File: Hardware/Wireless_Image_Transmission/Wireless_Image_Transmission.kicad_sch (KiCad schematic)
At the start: 66 parts, among them IC1 EA3036QBR, IC10 HY2213-BB3A, IC11 HY2213-BB3A, IC12 HY2213-BB3A, IC13 HY2213-BB3A, IC2 TPS5450DDAR, Q2 AO3401A, Q3 AO3400, Q4 AO3400, Q5 AO3400, Q6 AO3400

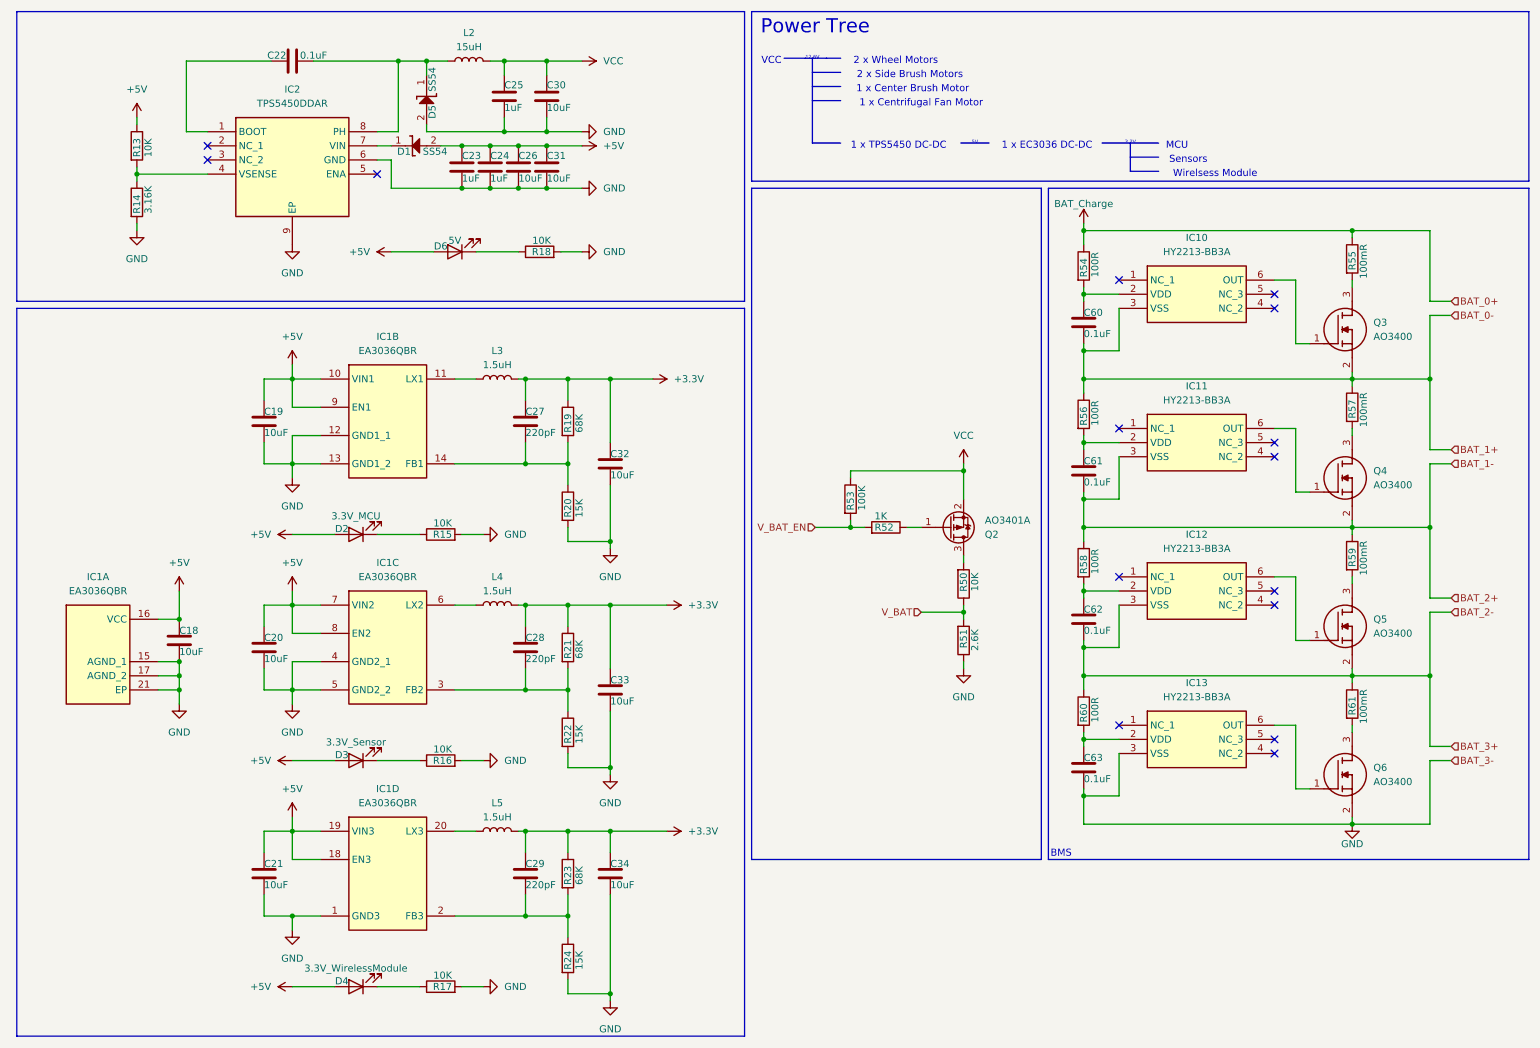
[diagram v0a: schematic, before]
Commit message: Add Image Transmission
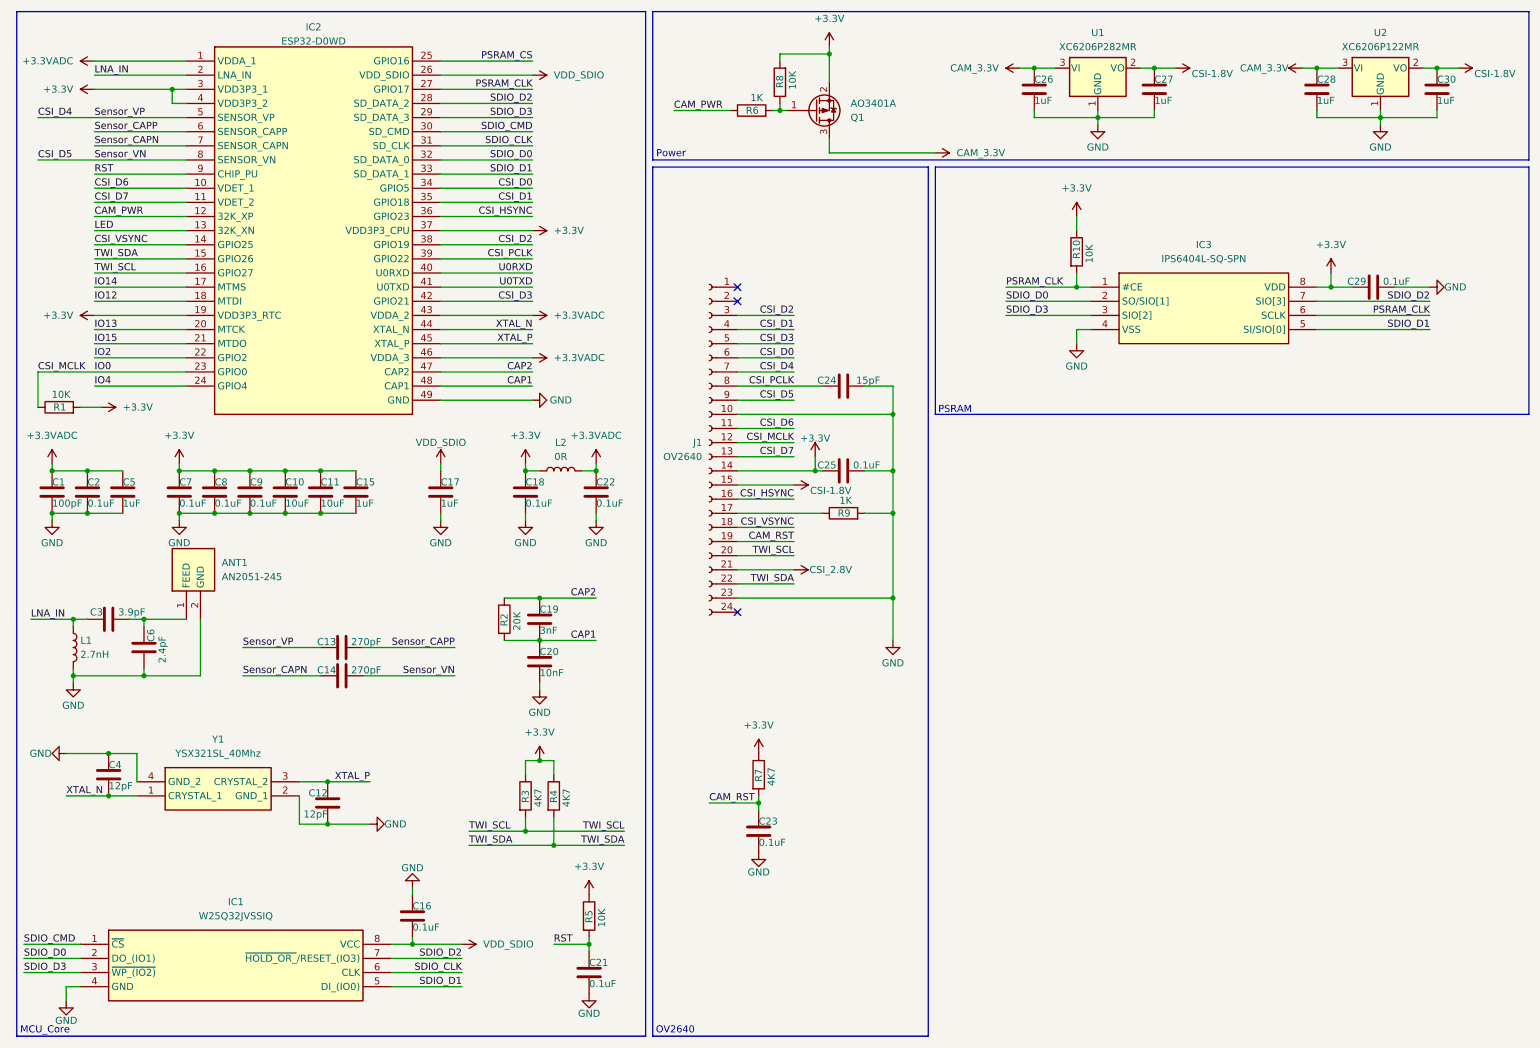
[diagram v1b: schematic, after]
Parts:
- removed C31, C32, C33, C34: 10uF, symbol Device:C
- removed C60, C61, C62, C63: 0.1uF, symbol Device:C
- removed D1, D5: SS54, DIOM5126X245N, symbol SamacSys_Parts:SS54
- removed D2: 3.3V_MCU, symbol Device:LED
- removed D3: 3.3V_Sensor, symbol Device:LED
- removed D4: 3.3V_WirelessModule, symbol Device:LED
- removed D6: 5V, symbol Device:LED
- removed IC1: EA3036QBR, QFN40P300X300X80-21N, symbol SamacSys_Parts:EA3036QBR
- removed IC10, IC11, IC12, IC13: HY2213-BB3A, SOT95P280X140-6N, symbol SamacSys_Parts:HY2213-BB3A
- removed IC2: TPS5450DDAR, SOIC127P600X170-9N, symbol SamacSys_Parts:TPS5450DDAR
- removed L3, L4, L5: 1.5uH, symbol Device:L
- removed Q2: AO3401A, Package_TO_SOT_SMD:SOT-23, symbol Transistor_FET:AO3401A
- removed Q3, Q4, Q5, Q6: AO3400, SOT95P280X125-3N, symbol SamacSys_Parts:AO3400
- removed R13, R15, R16, R17, R18, R50: 10K, symbol Device:R
- removed R14: 3.16K, symbol Device:R
- removed R19, R21, R23: 68K, symbol Device:R
- removed R20, R22, R24: 15K, symbol Device:R
- removed R51: 2.6K, symbol Device:R
- removed R52: 1K, symbol Device:R
- removed R53: 100K, symbol Device:R
- removed R54, R56, R58, R60: 100R, symbol Device:R
- removed R55, R57, R59, R61: 100mR, symbol Device:R
- added ANT1: AN2051-245, ANTC5020X127N, symbol SamacSys_Parts:AN2051-245
- added C1: 100pF, Capacitor_SMD:C_0402_1005Metric, symbol Device:C
- added C10, C11: 10uF, Capacitor_SMD:C_0402_1005Metric, symbol Device:C
- added C12, C4: 12pF, Capacitor_SMD:C_0402_1005Metric, symbol Device:C
- added C13, C14: 270pF, Capacitor_SMD:C_0402_1005Metric, symbol Device:C
- added C15, C17, C5: 1uF, Capacitor_SMD:C_0402_1005Metric, symbol Device:C
- added C16, C2, C7, C8, C9: 0.1uF, Capacitor_SMD:C_0402_1005Metric, symbol Device:C
- added C3: 3.9pF, Capacitor_SMD:C_0402_1005Metric, symbol Device:C
- added C6: 2.4pF, Capacitor_SMD:C_0402_1005Metric, symbol Device:C
- added IC1: W25Q32JVSSIQ, SOIC127P790X216-8N, symbol SamacSys_Parts:W25Q32JVSSIQ
- added IC2: ESP32-D0WD, QFN40P600X600X90-49N-D, symbol SamacSys_Parts:ESP32-D0WD
- added IC3: IPS6404L-SQ-SPN, SOIC127P600X175-8N, symbol SamacSys_Parts:IPS6404L-SQ-SPN
- added J1: OV2640, Connector_FFC-FPC:TE_2-1734839-4_1x24-1MP_P0.5mm_Horizontal, symbol Connector:Conn_01x24_Socket
- added L1: 2.7nH, Inductor_SMD:L_0402_1005Metric_Pad0.77x0.64mm_HandSolder, symbol Device:L
- added Q1: AO3401A, Package_TO_SOT_SMD:SOT-23, symbol Transistor_FET:AO3401A
- added R1, R10, R5, R8: 10K, Resistor_SMD:R_0402_1005Metric, symbol Device:R
- added R2: 20K, Resistor_SMD:R_0402_1005Metric, symbol Device:R
- added R3, R4, R7: 4K7, Resistor_SMD:R_0402_1005Metric, symbol Device:R
- added R6, R9: 1K, Resistor_SMD:R_0402_1005Metric, symbol Device:R
- added U1: XC6206P282MR, Package_TO_SOT_SMD:SOT-23-3, symbol Regulator_Linear:XC6206PxxxMR
- added U2: XC6206P122MR, Package_TO_SOT_SMD:SOT-23-3, symbol Regulator_Linear:XC6206PxxxMR
- added Y1: YSX321SL_40Mhz, YSX321SL, symbol SamacSys_Parts:YSX321SL
- C18, C21: value 10uF -> 0.1uF; footprint (none) -> Capacitor_SMD:C_0402_1005Metric
- C19: value 10uF -> 3nF; footprint (none) -> Capacitor_SMD:C_0402_1005Metric
- C20: value 10uF -> 10nF; footprint (none) -> Capacitor_SMD:C_0402_1005Metric
- C22: footprint (none) -> Capacitor_SMD:C_0402_1005Metric
- C23, C25: value 1uF -> 0.1uF; footprint (none) -> Capacitor_SMD:C_0402_1005Metric
- C24: value 1uF -> 15pF; footprint (none) -> Capacitor_SMD:C_0402_1005Metric
- C26, C30: value 10uF -> 1uF; footprint (none) -> Capacitor_SMD:C_0603_1608Metric
- C27, C28: value 220pF -> 1uF; footprint (none) -> Capacitor_SMD:C_0603_1608Metric
- C29: value 220pF -> 0.1uF; footprint (none) -> Capacitor_SMD:C_0402_1005Metric
- L2: value 15uH -> 0R; footprint (none) -> Inductor_SMD:L_0402_1005Metric_Pad0.77x0.64mm_HandSolder
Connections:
- net +3.3V: now also C18.1, C25.1, L2.1, C10.1, C11.1, C15.1, C7.1, C8.1, C9.1, IC2.19 (VDD3P3_RTC), IC2.3 (VDD3P3_1), IC2.37 (VDD3P3_CPU), IC2.4 (VDD3P3_2), IC3.8 (VDD), J1.14 (Pin_14), Q1.2 (S), R1.2, R10.1, R3.1, R4.1, R5.1, R7.1, R8.2; no longer C27.1, C28.1
- net GND: now also C22.2, C27.2, C28.2, C29.2, ANT1.2 (GND), C1.2, C10.2, C11.2, C12.2, C15.2, C16.1, C17.2, C2.2, C4.1, C5.2, C6.2, C7.2, C8.2, C9.2, IC1.4 (GND), IC2.49 (GND), IC3.4 (VSS), J1.10 (Pin_10), J1.23 (Pin_23), L1.2, R9.2, U1.1 (GND), U2.1 (GND), Y1.2 (GND_1), Y1.4 (GND_2); no longer C19.2
- net +3.3VADC: now reaches C22.1
- net +3.3VADC: now also L2.2, C1.1, C2.1, C5.1, IC2.1 (VDDA_1), IC2.43 (VDDA_2), IC2.46 (VDDA_3)
- removed net +5V: C18.1, C19.1, C20.1, C21.1, C23.1, C24.1, C26.1
- removed net VCC: C25.1, C30.1, L2.2
- new net: Q1.1 (G), R6.2, R8.1
- new net: ANT1.1 (FEED), C3.2, C6.1
- new net: J1.17 (Pin_17), R9.1
- new net CAM_3.3V: C26.1, C28.1, Q1.3 (D), U1.3 (VI), U2.3 (VI)
- new net CAM_PWR: IC2.12 (32K_XP), R6.1
- new net CAM_RST: C23.1, J1.19 (Pin_19), R7.2
- new net CAP1: C19.2, C20.1, IC2.48 (CAP1), R2.2
- new net CAP2: C19.1, IC2.47 (CAP2), R2.1
- new net CSI-1.8V: C27.1, C30.1, J1.15 (Pin_15), U1.2 (VO), U2.2 (VO)
- new net CSI_2.8V: J1.21 (Pin_21)
- new net CSI_D0: IC2.34 (GPIO5), J1.6 (Pin_6)
- new net CSI_D1: IC2.35 (GPIO18), J1.4 (Pin_4)
- new net CSI_D2: IC2.38 (GPIO19), J1.3 (Pin_3)
- new net CSI_D3: IC2.42 (GPIO21), J1.5 (Pin_5)
- new net CSI_D4: C13.1, IC2.5 (SENSOR_VP), J1.7 (Pin_7)
- new net CSI_D5: C14.2, IC2.8 (SENSOR_VN), J1.9 (Pin_9)
- new net CSI_D6: IC2.10 (VDET_1), J1.11 (Pin_11)
- new net CSI_D7: IC2.11 (VDET_2), J1.13 (Pin_13)
- new net CSI_HSYNC: IC2.36 (GPIO23), J1.16 (Pin_16)
- new net CSI_MCLK: IC2.23 (GPIO0), J1.12 (Pin_12), R1.1
- new net CSI_PCLK: C24.1, IC2.39 (GPIO22), J1.8 (Pin_8)
- new net CSI_VSYNC: IC2.14 (GPIO25), J1.18 (Pin_18)
- new net IO12: IC2.18 (MTDI)
- new net IO13: IC2.20 (MTCK)
- new net IO14: IC2.17 (MTMS)
- new net IO15: IC2.21 (MTDO)
- new net IO2: IC2.22 (GPIO2)
- new net IO4: IC2.24 (GPIO4)
- new net LED: IC2.13 (32K_XN)
- new net LNA_IN: C3.1, IC2.2 (LNA_IN), L1.1
- new net PSRAM_CLK: IC2.27 (GPIO17), IC3.1 (#CE), IC3.6 (SCLK), R10.2
- new net PSRAM_CS: IC2.25 (GPIO16)
- new net RST: C21.1, IC2.9 (CHIP_PU), R5.2
- new net SDIO_CLK: IC1.6 (CLK), IC2.31 (SD_CLK)
- new net SDIO_CMD: IC1.1 (~{CS}), IC2.30 (SD_CMD)
- new net SDIO_D0: IC1.2 (DO_(IO1)), IC2.32 (SD_DATA_0), IC3.2 (SO/SIO[1])
- new net SDIO_D1: IC1.5 (DI_(IO0)), IC2.33 (SD_DATA_1), IC3.5 (SI/SIO[0])
- new net SDIO_D2: IC1.7 (~{HOLD_OR_}/RESET_(IO3)), IC2.28 (SD_DATA_2), IC3.7 (SIO[3])
- new net SDIO_D3: IC1.3 (~{WP_(IO2)}), IC2.29 (SD_DATA_3), IC3.3 (SIO[2])
- new net Sensor_CAPN: C14.1, IC2.7 (SENSOR_CAPN)
- new net Sensor_CAPP: C13.2, IC2.6 (SENSOR_CAPP)
- new net TWI_SCL: IC2.16 (GPIO27), J1.20 (Pin_20), R3.2
- new net TWI_SDA: IC2.15 (GPIO26), J1.22 (Pin_22), R4.2
- new net U0RXD: IC2.40 (U0RXD)
- new net U0TXD: IC2.41 (U0TXD)
- new net VDD_SDIO: C16.2, C17.1, IC1.8 (VCC), IC2.26 (VDD_SDIO)
- new net XTAL_N: C4.2, IC2.44 (XTAL_N), Y1.1 (CRYSTAL_1)
- new net XTAL_P: C12.1, IC2.45 (XTAL_P), Y1.3 (CRYSTAL_2)
- no-connect marks 15 -> 3
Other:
- note added: "MCU_Core"
- note added: "OV2640"
- note added: "PSRAM"
- note added: "Power"
- note removed: "1 x Center Brush Motor"
- note removed: "1 x Centrifugal Fan Motor"
- note removed: "1 x EC3036 DC-DC"
- note removed: "1 x TPS5450 DC-DC"
- note removed: "12.6V"
- note removed: "2 x Side Brush Motors"
- note removed: "2 x Wheel Motors"
- note removed: "3.3V"
- note removed: "5V"
- note removed: "BMS"
- note removed: "MCU"
- note removed: "Power Tree"
- note removed: "Sensors"
- note removed: "VCC"
- note removed: "Wirelsess Module"
- title: Power_Manager -> (none)

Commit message: Update PCB
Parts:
- added JP1: EN, Jumper:SolderJumper-2_P1.3mm_Open_RoundedPad1.0x1.5mm, symbol Jumper:Jumper_2_Open
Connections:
- net CSI_2.8V: now also C27.1, U1.2 (VO)
- net CSI_MCLK: now also JP1.1 (A)
- net GND: now also JP1.2 (B)
- net PSRAM_CLK: no longer IC3.1 (#CE), R10.2
- net PSRAM_CS: now also IC3.1 (#CE), R10.2
- net CSI-1.8V renamed CSI_1.8V
- net CSI_1.8V: no longer C27.1, U1.2 (VO)
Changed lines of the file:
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@@
 	(wire
 		(pts
+			(xy 76.2 139.7) (xy 91.44 139.7)
+		)
+		(stroke
+			(width 0)
+			(type default)
+		)
+	)
+	(wire
+		(pts
 			(xy 26.67 41.91) (xy 43.18 41.91)
 		)
@@
 	(wire
 		(pts
+			(xy 53.34 139.7) (xy 66.04 139.7)
+		)
+		(stroke
+			(width 0)
+			(type default)
+		)
+	)
+	(wire
+		(pts
 			(xy 83.82 179.07) (xy 83.82 180.34)
 		)
@@
 		)
 	)
-	(label "PSRAM_CLK"
-		(at 190.5 62.23 0)
-		(fields_autoplaced yes)
-		(effects
-			(font
-				(size 1.27 1.27)
-			)
-			(justify left bottom)
-		)
-	)
 	(label "Sensor_VP"
 		(at 26.67 31.75 0)
@@
 		)
 	)
+	(label "IO0"
+		(at 53.34 139.7 0)
+		(fields_autoplaced yes)
+		(effects
+			(font
+				(size 1.27 1.27)
+			)
+			(justify left bottom)
+		)
+	)
 	(label "CSI_D5"
 		(at 152.4 82.55 180)
@@
 		)
 	)
+	(label "PSRAM_CS"
+		(at 190.5 62.23 0)
+		(fields_autoplaced yes)
+		(effects
+			(font
+				(size 1.27 1.27)
+			)
+			(justify left bottom)
+		)
+	)
 	(label "CSI_D2"
 		(at 152.4 67.31 180)
@@
 			)
 		)
-		(property "Value" "CSI-1.8V"
+		(property "Value" "CSI_1.8V"
 			(at 278.384 23.876 90)
 			(effects
@@
 			)
 		)
-		(property "Value" "CSI-1.8V"
+		(property "Value" "CSI_1.8V"
 			(at 159.004 98.806 90)
 			(effects
@@
 			)
 		)
-		(property "Value" "CSI-1.8V"
+		(property "Value" "CSI_2.8V"
 			(at 227.584 23.876 90)
 			(effects
@@
 	)
 	(symbol
+		(lib_id "Jumper:Jumper_2_Open")
+		(at 71.12 139.7 0)
+		(unit 1)
+		(exclude_from_sim yes)
+		(in_bom yes)
+		(on_board yes)
+		(dnp no)
+		(property "Reference" "JP1"
+			(at 71.12 141.478 0)
+			(effects
+				(font
+					(size 1.27 1.27)
+				)
+			)
+		)
+		(property "Value" "EN"
+			(at 71.12 135.89 0)
+			(effects
+				(font
+					(size 1.27 1.27)
+				)
+			)
+		)
+		(property "Footprint" "Jumper:SolderJumper-2_P1.3mm_Open_RoundedPad1.0x1.5mm"
+			(at 71.12 139.7 0)
+			(effects
+				(font
+					(size 1.27 1.27)
+				)
+				(hide yes)
+			)
+		)
+		(property "Datasheet" "~"
+			(at 71.12 139.7 0)
+			(effects
+				(font
+					(size 1.27 1.27)
+				)
+				(hide yes)
+			)
+		)
+		(property "Description" "Jumper, 2-pole, open"
+			(at 71.12 139.7 0)
+			(effects
+				(font
+					(size 1.27 1.27)
+				)
+				(hide yes)
+			)
+		)
+		(pin "2"
+		)
+		(pin "1"
+		)
+		(instances
+			(project ""
+				(path "/44ec32b6-3d46-42e8-ab46-0a044570255b"
+					(reference "JP1")
+					(unit 1)
+				)
+			)
+		)
+	)
+	(symbol
 		(lib_id "Device:C")
 		(at 161.29 95.25 90)
@@
 					(unit 1)
 				)
+			)
+		)
+	)
+	(symbol
+		(lib_id "power:GND")
+		(at 91.44 139.7 90)
+		(mirror x)
+		(unit 1)
+		(exclude_from_sim no)
+		(in_bom yes)
+		(on_board yes)
+		(dnp no)
+		(property "Reference" "#PWR048"
+			(at 97.79 139.7 0)
+			(effects
+				(font
+					(size 1.27 1.27)
+				)
+				(hide yes)
+			)
+		)
+		(property "Value" "GND"
+			(at 96.012 139.7 90)
+			(effects
+				(font
+					(size 1.27 1.27)
+				)
+			)
+		)
+		(property "Footprint" ""
+			(at 91.44 139.7 0)
+			(effects
+				(font
+					(size 1.27 1.27)
+				)
+				(hide yes)
+			)
+		)
+		(property "Datasheet" ""
+			(at 91.44 139.7 0)
+			(effects
+				(font
+					(size 1.27 1.27)
+				)
+				(hide yes)
+			)
+		)
+		(property "Description" "Power symbol creates a global label with name \"GND\" , ground"
+			(at 91.44 139.7 0)
+			(effects
+				(font
+					(size 1.27 1.27)
+				)
+				(hide yes)
+			)
+		)
+		(pin "1"
+		)
+		(instances
+			(project "Wireless_Image_Transmission"
+				(path "/44ec32b6-3d46-42e8-ab46-0a044570255b"
+					(reference "#PWR048")
+					(unit 1)
+				)
